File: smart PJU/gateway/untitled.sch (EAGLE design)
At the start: 9 parts, among them J1 U.FL-R-SMT(01), U1 ESP32-DEVKITC-32D, X1 MSTBA2

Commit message: membuat PCB gateway
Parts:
- removed X1: MSTBA2, con-phoenix-508:MSTBA2
- added C10, C11, C13: 10uF, rcl:C-EUC0805K
- added C12: UPM2E100MHD1TO, UPM2E100MHD1TO:UPM2E100MHD1TO
- added C14, C7: 1uF, rcl:C-EUC0805K
- added C15: (no value), rcl:CPOL-EU153CLV-0505
- added C3, C4: (no value), rcl:C-EUC0805K
- added C5, C6: 22pF, rcl:C-EUC0805K
- added C8: 10uF, rcl:CPOL-EU153CLV-0505
- added C9: 100nF, rcl:C-EUC0805K
- added D1, D2: 1N5819HW-7, 1N5819HW-7:1N5819HW-7
- added D18, D19, D20: SML-LXT0805IW-TR, SML-LXT0805IW-TR:SML-LXT0805IW-TR
- added J2: 10118193-0001LF, 10118193-0001LF:10118193-0001LF
- added MD1: ESPRESSIF_SYSTEMS_ESP32-WROOM-32U_16MBESPRESSIF_SYSTEMS_ESP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, Espressif Systems - ESP32-WROOM-32U (16MB):ESPRESSIF_SYSTEMS_ESP32-WROOM-32U_16MBESPRESSIF_SYSTEMS_ESP32-WROOM-32U_16MB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
- added MINI1: (no value), mini360:MINI360
- added Q16, Q17: MMBT3904, MMBT3904:MMBT3904
- added Q18: 12MHz, crystal:CRYSTALSM49
- added R41, R42, R43, R44, R45, R46, R47: 10k, rcl:R-EU_R0805
- added S1, S2: (no value), switch-omron:31-XX
- added TB7.1: (no value), TB7.62:TB7.62
- added U19: CH340G, CH340G:CH340G
- C1: value (none) -> 10uF
- C2: value (none) -> 100nF
- U1: value ESP32-DEVKITC-32D -> AMS1117; device ESP32-DEVKITC-32D:ESP32-DEVKITC-32D -> AMS1117:AMS1117
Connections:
- new net DTR: Q17.E, R41.1, U19.!DTR
- new net EN: C3.1, MD1.EN, Q16.C, R43.1, S1.P
- new net IO0: C4.1, MD1.IO0, Q17.C, R44.1, S2.P
- new net N$102: C5.2, Q18.2, U19.XI
- new net N$103: C6.2, Q18.1, U19.XO
- new net N$104: C9.2, U19.V3
- new net N$105: D18.A, R45.1
- new net N$106: D19.A, R46.1
- new net N$107: D20.A, R47.1
- new net N$11: Q17.B, R42.2
- new net N$3: D1.A, PS1.+VO
- new net N$5: C13.2, C14.2, C15.+, MINI1.OUT+, SIM800L1.VCC
- new net N$99: Q16.B, R41.2
- new net RTS: Q16.E, R42.1, U19.!RTS
- new net RX: D19.C, MD1.TXD0, U19.RXD
- new net TX: D18.C, MD1.RXD0, U19.TXD
- new net USB_N: J2.D-, U19.UD-
- new net USB_P: J2.D+, U19.UD+
- new net VCC_USB: C7.2, C8.+, D2.A, J2.VUSB, U19.VCC
- net 3V3: now also C10.2, MD1.3V3, R43.2, R44.2, R45.2, R46.2, U1.VOUT; no longer U1.3V3
- net GND: now also C10.1, C11.1, C13.1, C14.1, C15.-, C3.2, C4.2, C5.1, C6.1, C7.1, C8.-, C9.1, D20.C, J2.GND, J2.SHIELD, MD1.1_GND, MD1.2_GND, MD1.3_GND, MD1.4_GND, MINI1.IN-, MINI1.OUT-, S1.S, S2.S, U1.ADJ/GND, U19.GND; no longer U1.GND1
- net LORA_DI0: now also MD1.IO25; no longer U1.IO25
- net LORA_DI1: now also MD1.IO32; no longer U1.IO32
- net MISO_VSPI: now also MD1.IO19; no longer U1.IO19
- net MOSI_VSPI: now also MD1.IO23; no longer U1.IO23
- net N$1: now also C12.P, TB7.1.T2; no longer X1-1.1
- net N$2: now also C12.N, TB7.1.T1; no longer X1-2.1
- net RST_LORA: now also MD1.IO26; no longer U1.IO26
- net RX_SIM: now also MD1.IO17; no longer U1.IO16
- net SCK_VSPI: now also MD1.IO18; no longer U1.IO18
- net SCL: now also MD1.IO22; no longer U1.IO22
- net SDA: now also MD1.IO21; no longer U1.IO21
- net SS_LORA: now also MD1.IO5; no longer U1.IO5
- net TX_SIM: now also MD1.IO16; no longer U1.IO17
- net VCC: now also C11.2, D1.K, D2.K, MINI1.IN+, R47.2, U1.VIN; no longer PS1.+VO, U1.EXT_5V
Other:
- moved on the sheet: C1, C2, J1, PS1

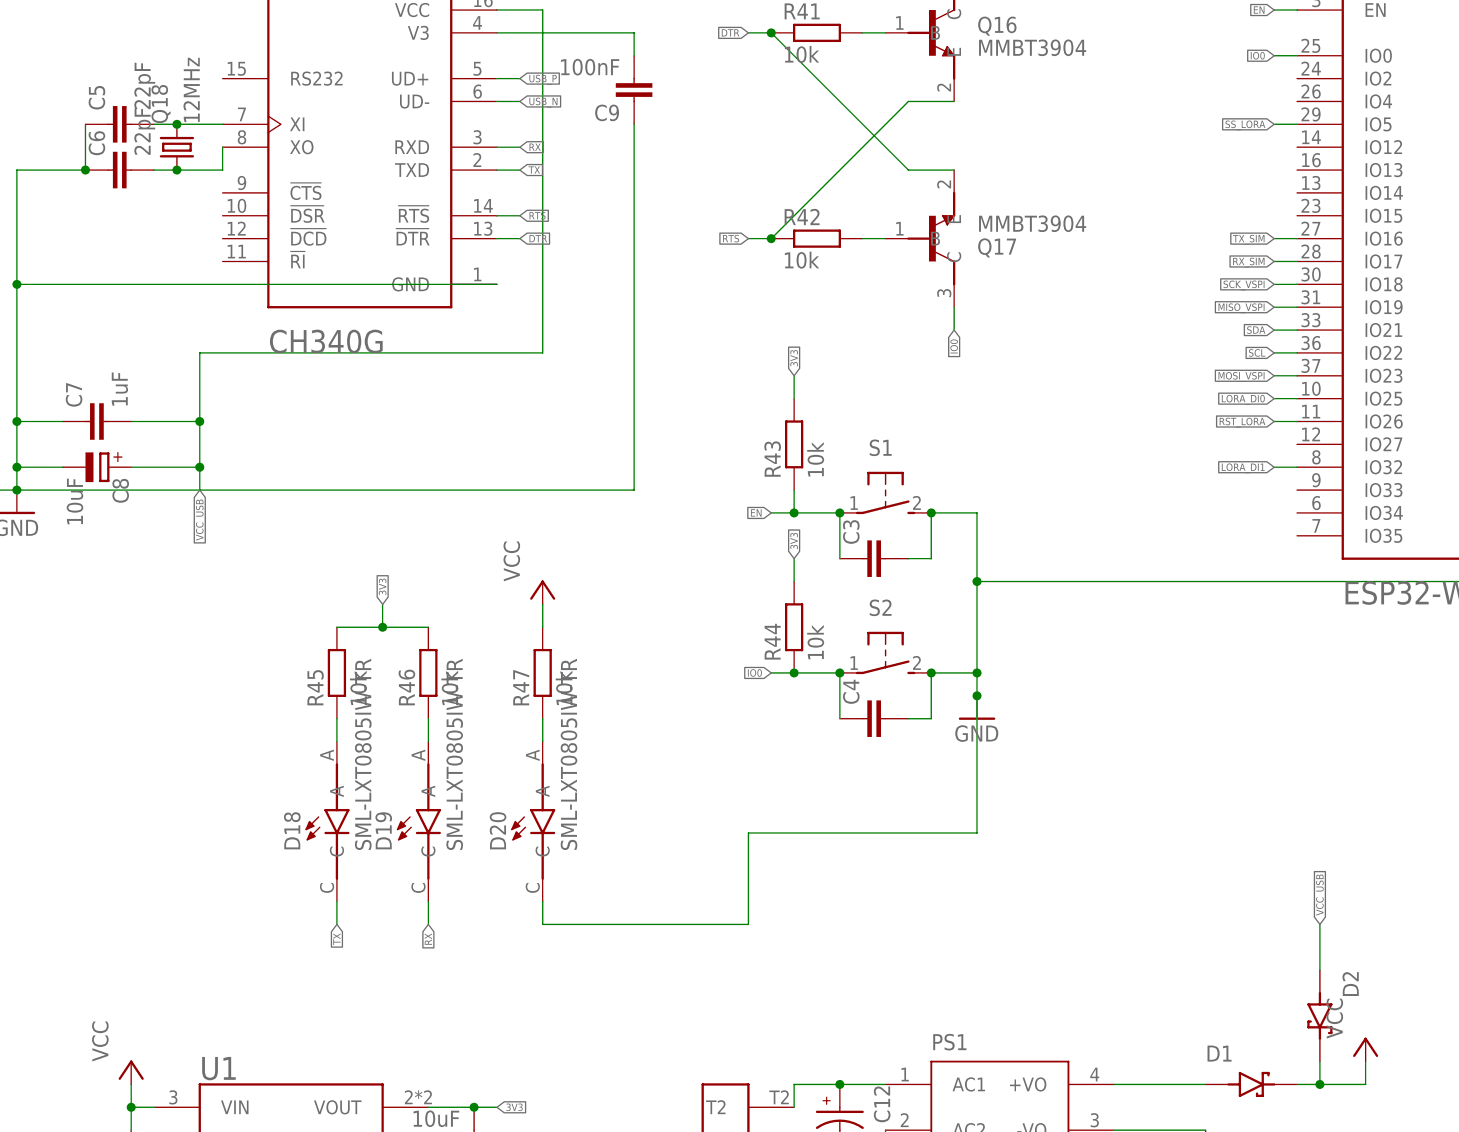
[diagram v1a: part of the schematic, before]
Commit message: revisi relay node dan list komponen
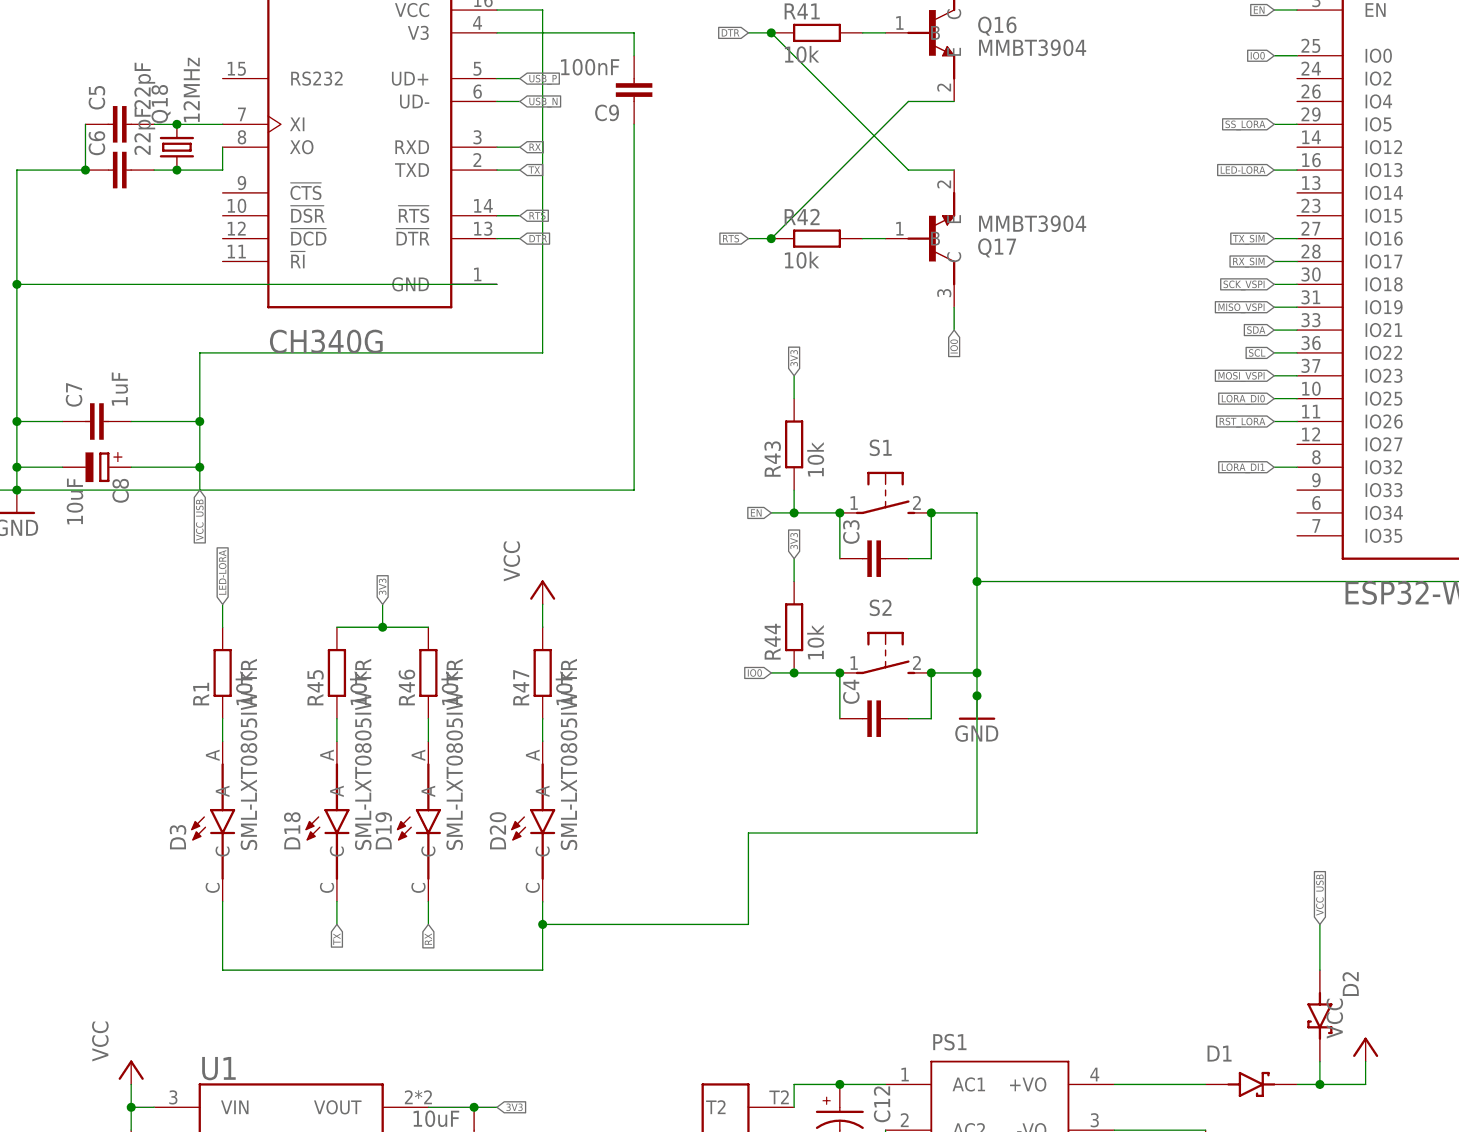
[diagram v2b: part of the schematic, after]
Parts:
- added D3: SML-LXT0805IW-TR, SML-LXT0805IW-TR:SML-LXT0805IW-TR
- added R1: 10k, rcl:R-EU_R0805
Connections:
- new net LED-LORA: MD1.IO13, R1.2
- new net N$7: D3.A, R1.1
- net GND: now also D3.C
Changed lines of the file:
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@@
 <part name="C14" library="rcl" library_urn="urn:adsk.eagle:library:334" deviceset="C-EU" device="C0805K" package3d_urn="urn:adsk.eagle:package:23681/2" value="1uF"/>
 <part name="C15" library="rcl" library_urn="urn:adsk.eagle:library:334" deviceset="CPOL-EU" device="153CLV-0505" package3d_urn="urn:adsk.eagle:package:23402/2"/>
+<part name="D3" library="SML-LXT0805IW-TR" deviceset="SML-LXT0805IW-TR" device=""/>
+<part name="R1" library="rcl" library_urn="urn:adsk.eagle:library:334" deviceset="R-EU_" device="R0805" package3d_urn="urn:adsk.eagle:package:23553/2" value="10k"/>
 </parts>
 <sheets>
@@
 <attribute name="NAME" x="186.563" y="236.7026" size="1.778" layer="95"/>
 <attribute name="VALUE" x="186.563" y="231.6226" size="1.778" layer="96"/>
+</instance>
+<instance part="D3" gate="G$1" x="73.66" y="287.02" smashed="yes" rot="R90">
+<attribute name="NAME" x="69.58973125" y="284.98486875" size="1.780740625" layer="95" rot="R90"/>
+<attribute name="VALUE" x="77.47315" y="284.98631875" size="1.77946875" layer="96" rot="R90"/>
+</instance>
+<instance part="R1" gate="G$1" x="73.66" y="304.8" smashed="yes" rot="R90">
+<attribute name="NAME" x="72.1614" y="300.99" size="1.778" layer="95" rot="R90"/>
+<attribute name="VALUE" x="76.962" y="300.99" size="1.778" layer="96" rot="R90"/>
 </instance>
 </instances>
@@
 <wire x1="132.08" y1="276.86" x2="109.22" y2="276.86" width="0.1524" layer="91"/>
 <wire x1="109.22" y1="276.86" x2="109.22" y2="279.4" width="0.1524" layer="91"/>
+<pinref part="D3" gate="G$1" pin="C"/>
+<wire x1="73.66" y1="279.4" x2="73.66" y2="271.78" width="0.1524" layer="91"/>
+<wire x1="73.66" y1="271.78" x2="109.22" y2="271.78" width="0.1524" layer="91"/>
+<wire x1="109.22" y1="271.78" x2="109.22" y2="276.86" width="0.1524" layer="91"/>
+<junction x="109.22" y="276.86"/>
 </segment>
 <segment>
@@
 </segment>
 </net>
+<net name="LED-LORA" class="0">
+<segment>
+<pinref part="MD1" gate="G$0" pin="IO13"/>
+<wire x1="193.04" y1="360.68" x2="190.5" y2="360.68" width="0.1524" layer="91"/>
+<label x="190.5" y="360.68" size="0.8128" layer="95" rot="R180" xref="yes"/>
+</segment>
+<segment>
+<pinref part="R1" gate="G$1" pin="2"/>
+<wire x1="73.66" y1="309.88" x2="73.66" y2="312.42" width="0.1524" layer="91"/>
+<label x="73.66" y="312.42" size="0.8128" layer="95" rot="R90" xref="yes"/>
+</segment>
+</net>
+<net name="N$7" class="0">
+<segment>
+<pinref part="D3" gate="G$1" pin="A"/>
+<pinref part="R1" gate="G$1" pin="1"/>
+<wire x1="73.66" y1="297.18" x2="73.66" y2="299.72" width="0.1524" layer="91"/>
+</segment>
+</net>

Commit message: revisi PS hilink 2A
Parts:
- removed PS1: HLK-5M05, HLK-5M05:HLK-5M05
- added PS2: HLK-10M05, HLK-10M05:HLK-10M05
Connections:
- net GND: now also PS2.-V0; no longer PS1.-VO
- net N$1: now also PS2.AC_1; no longer PS1.AC1
- net N$2: now also PS2.AC_2; no longer PS1.AC2
- net N$3: now also PS2.+V0; no longer PS1.+VO
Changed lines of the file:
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@@
 <part name="P+5" library="supply1" library_urn="urn:adsk.eagle:library:371" deviceset="VCC" device=""/>
 <part name="C11" library="rcl" library_urn="urn:adsk.eagle:library:334" deviceset="C-EU" device="C0805K" package3d_urn="urn:adsk.eagle:package:23681/2" value="10uF"/>
-<part name="PS1" library="HLK-5M05" deviceset="HLK-5M05" device=""/>
 <part name="C12" library="UPM2E100MHD1TO" deviceset="UPM2E100MHD1TO" device=""/>
 <part name="D1" library="1N5819HW-7" deviceset="1N5819HW-7" device=""/>
@@
 <part name="D3" library="SML-LXT0805IW-TR" deviceset="SML-LXT0805IW-TR" device=""/>
 <part name="R1" library="rcl" library_urn="urn:adsk.eagle:library:334" deviceset="R-EU_" device="R0805" package3d_urn="urn:adsk.eagle:package:23553/2" value="10k"/>
+<part name="PS2" library="HLK-10M05" deviceset="HLK-10M05" device=""/>
 </parts>
 <sheets>
@@
 <attribute name="VALUE" x="61.976" y="253.619" size="1.778" layer="96" rot="R180"/>
 </instance>
-<instance part="PS1" gate="G$1" x="160.02" y="256.54" smashed="yes">
-<attribute name="NAME" x="152.4" y="262.89" size="1.778" layer="95"/>
-<attribute name="VALUE" x="152.4" y="248.92" size="1.778" layer="96"/>
-</instance>
 <instance part="C12" gate="G$1" x="142.24" y="256.54" smashed="yes" rot="R270">
 <attribute name="NAME" x="146.05" y="259.08" size="1.778" layer="95" rot="R270"/>
@@
 <attribute name="NAME" x="72.1614" y="300.99" size="1.778" layer="95" rot="R90"/>
 <attribute name="VALUE" x="76.962" y="300.99" size="1.778" layer="96" rot="R90"/>
+</instance>
+<instance part="PS2" gate="G$1" x="147.32" y="256.54" smashed="yes">
+<attribute name="NAME" x="171.45" y="264.16" size="1.778" layer="95" align="center-left"/>
+<attribute name="VALUE" x="171.45" y="261.62" size="1.778" layer="96" align="center-left"/>
 </instance>
 </instances>
@@
 </segment>
 <segment>
-<pinref part="PS1" gate="G$1" pin="-VO"/>
-<wire x1="172.72" y1="254" x2="182.88" y2="254" width="0.1524" layer="91"/>
-<pinref part="GND2" gate="1" pin="GND"/>
-</segment>
-<segment>
 <pinref part="RTC1" gate="G$1" pin="GND"/>
 <pinref part="GND1" gate="1" pin="GND"/>
@@
 <junction x="190.5" y="231.14"/>
 </segment>
+<segment>
+<pinref part="GND2" gate="1" pin="GND"/>
+<pinref part="PS2" gate="G$1" pin="-V0"/>
+<wire x1="182.88" y1="254" x2="182.88" y2="256.54" width="0.1524" layer="91"/>
+<wire x1="182.88" y1="256.54" x2="175.26" y2="256.54" width="0.1524" layer="91"/>
+</segment>
 </net>
 <net name="SCK_VSPI" class="0">
@@
 <net name="N$1" class="0">
 <segment>
-<pinref part="PS1" gate="G$1" pin="AC1"/>
 <pinref part="C12" gate="G$1" pin="P"/>
-<wire x1="147.32" y1="259.08" x2="142.24" y2="259.08" width="0.1524" layer="91"/>
 <pinref part="TB7.1" gate="G$1" pin="T2"/>
 <wire x1="142.24" y1="259.08" x2="137.16" y2="259.08" width="0.1524" layer="91"/>
 <wire x1="137.16" y1="259.08" x2="137.16" y2="256.54" width="0.1524" layer="91"/>
+<pinref part="PS2" gate="G$1" pin="AC_1"/>
+<wire x1="147.32" y1="256.54" x2="147.32" y2="259.08" width="0.1524" layer="91"/>
+<wire x1="147.32" y1="259.08" x2="142.24" y2="259.08" width="0.1524" layer="91"/>
 <junction x="142.24" y="259.08"/>
 </segment>
@@
 <net name="N$2" class="0">
 <segment>
-<pinref part="PS1" gate="G$1" pin="AC2"/>
 <pinref part="C12" gate="G$1" pin="N"/>
+<pinref part="TB7.1" gate="G$1" pin="T1"/>
+<wire x1="142.24" y1="251.46" x2="137.16" y2="251.46" width="0.1524" layer="91"/>
+<pinref part="PS2" gate="G$1" pin="AC_2"/>
 <wire x1="147.32" y1="254" x2="147.32" y2="251.46" width="0.1524" layer="91"/>
 <wire x1="147.32" y1="251.46" x2="142.24" y2="251.46" width="0.1524" layer="91"/>
 <junction x="142.24" y="251.46"/>
-<pinref part="TB7.1" gate="G$1" pin="T1"/>
-<wire x1="142.24" y1="251.46" x2="137.16" y2="251.46" width="0.1524" layer="91"/>
-</segment>
-</net>
-<net name="N$3" class="0">
-<segment>
-<pinref part="PS1" gate="G$1" pin="+VO"/>
-<wire x1="172.72" y1="259.08" x2="182.88" y2="259.08" width="0.1524" layer="91"/>
-<pinref part="D1" gate="G$1" pin="A"/>
 </segment>
 </net>
@@
 </segment>
 </net>
+<net name="N$3" class="0">
+<segment>
+<pinref part="D1" gate="G$1" pin="A"/>
+<wire x1="182.88" y1="259.08" x2="165.1" y2="259.08" width="0.1524" layer="91"/>
+<wire x1="165.1" y1="259.08" x2="165.1" y2="254" width="0.1524" layer="91"/>
+<pinref part="PS2" gate="G$1" pin="+V0"/>
+<wire x1="165.1" y1="254" x2="175.26" y2="254" width="0.1524" layer="91"/>
+</segment>
+</net>
